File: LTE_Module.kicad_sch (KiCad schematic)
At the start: 47 parts, among them J3 USB_C_Receptacle_USB2.0_14P, J4 SIM_Card_Shielded, Q3 FDN340P, Q4 DTC143Z, Q5 DTC143Z, Q6 DTC143Z, U6 TXB0104PW, U7 SIM7080G

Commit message: fixed layout
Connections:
- no-connect marks 25 -> 26
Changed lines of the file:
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@@
+	)
+	(no_connect
+		(at 60.96 50.8)
 	)
 	(no_connect

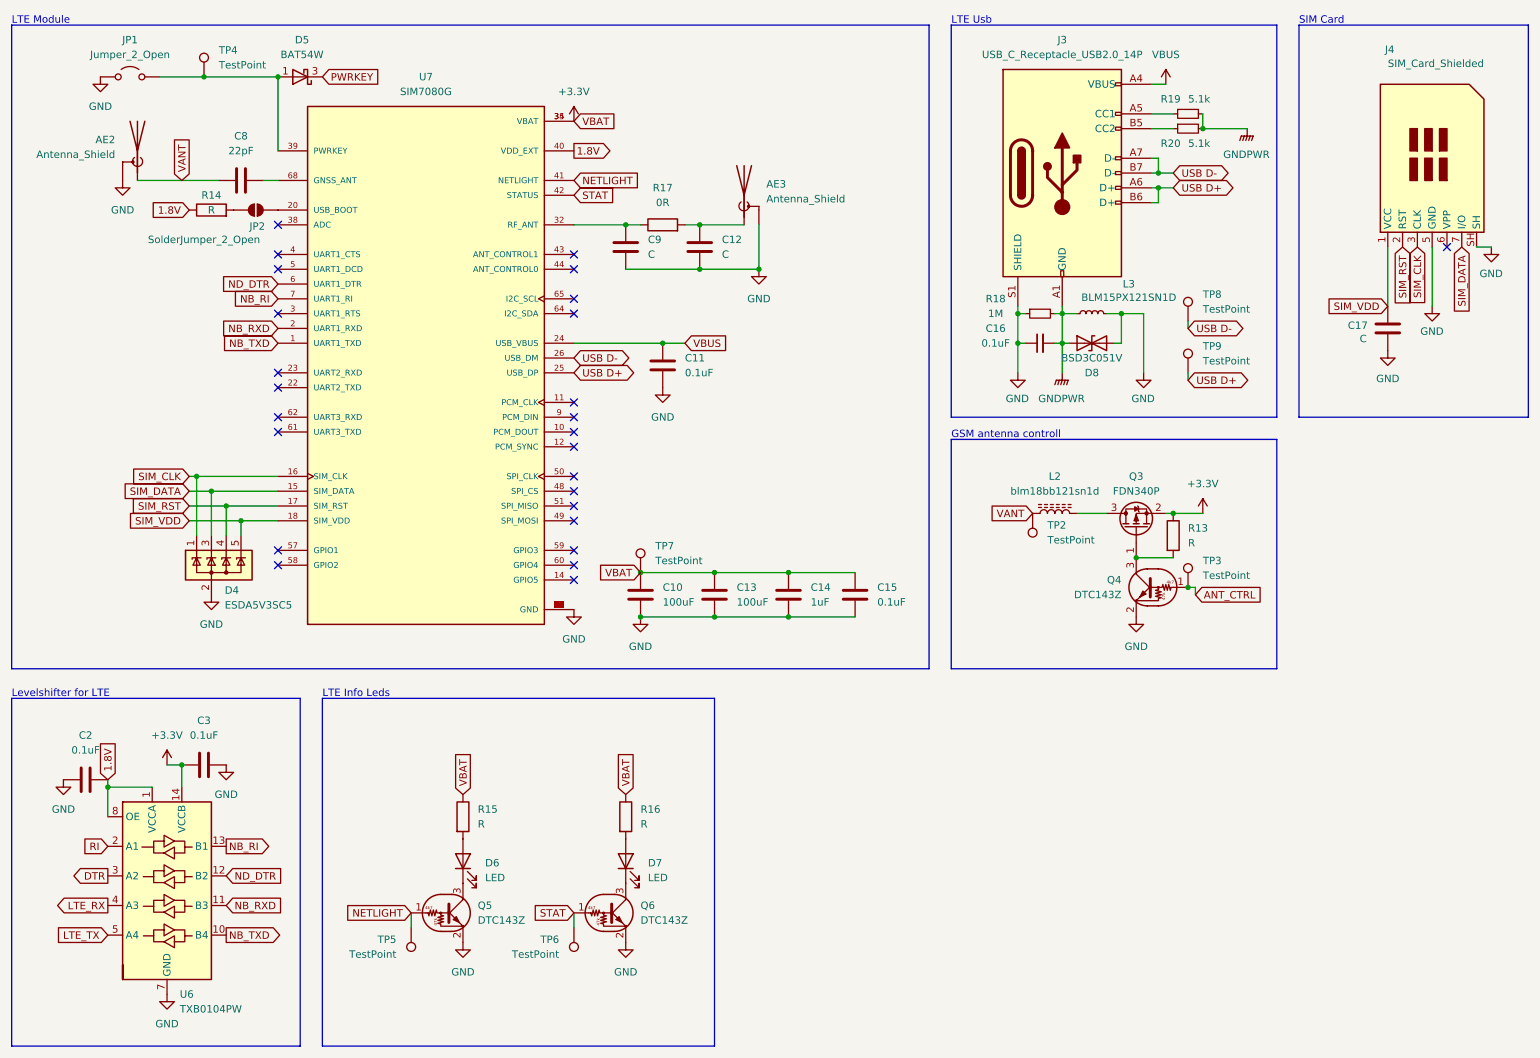
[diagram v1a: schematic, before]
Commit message: added psu and formated board outline
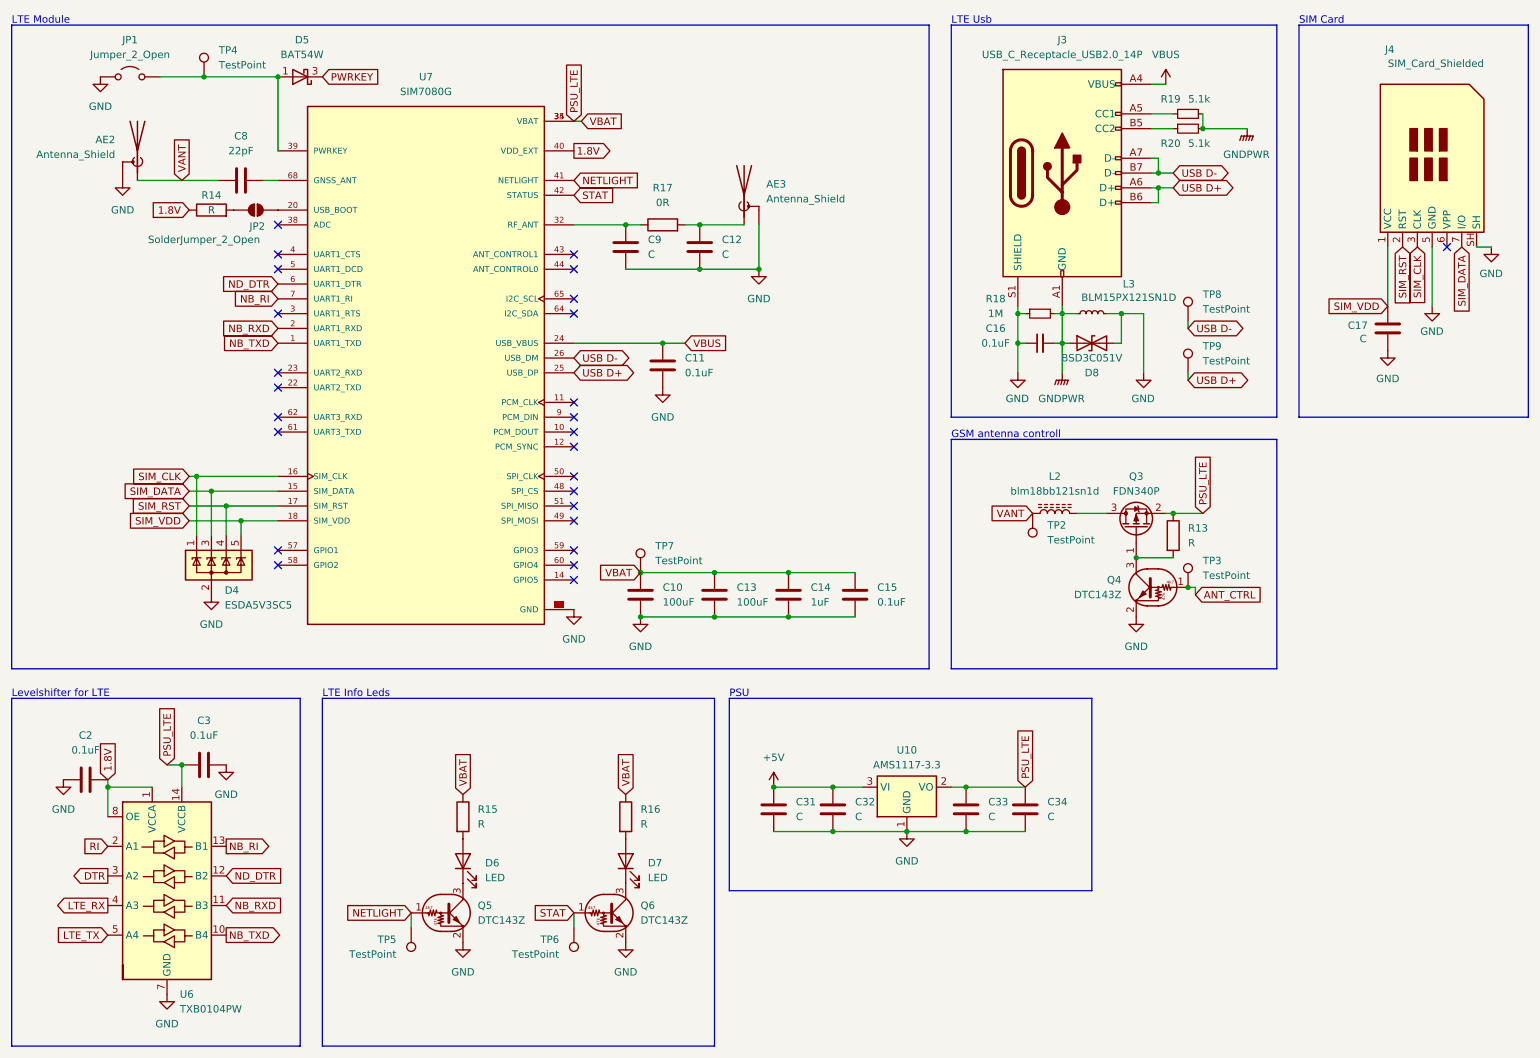
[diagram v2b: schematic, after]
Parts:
- added C31, C32, C33, C34: C, symbol Device:C
- added U10: AMS1117-3.3, Package_TO_SOT_SMD:SOT-223-3_TabPin2, symbol Regulator_Linear:AMS1117-3.3
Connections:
- net GND: now also C31.2, C32.2, C33.2, C34.2, U10.1 (GND)
- net +3.3V renamed PSU_LTE
- net PSU_LTE: now also C33.1, C34.1, U10.2 (VO)
- new net +5V: C31.1, C32.1, U10.3 (VI)
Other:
- note added: "PSU"

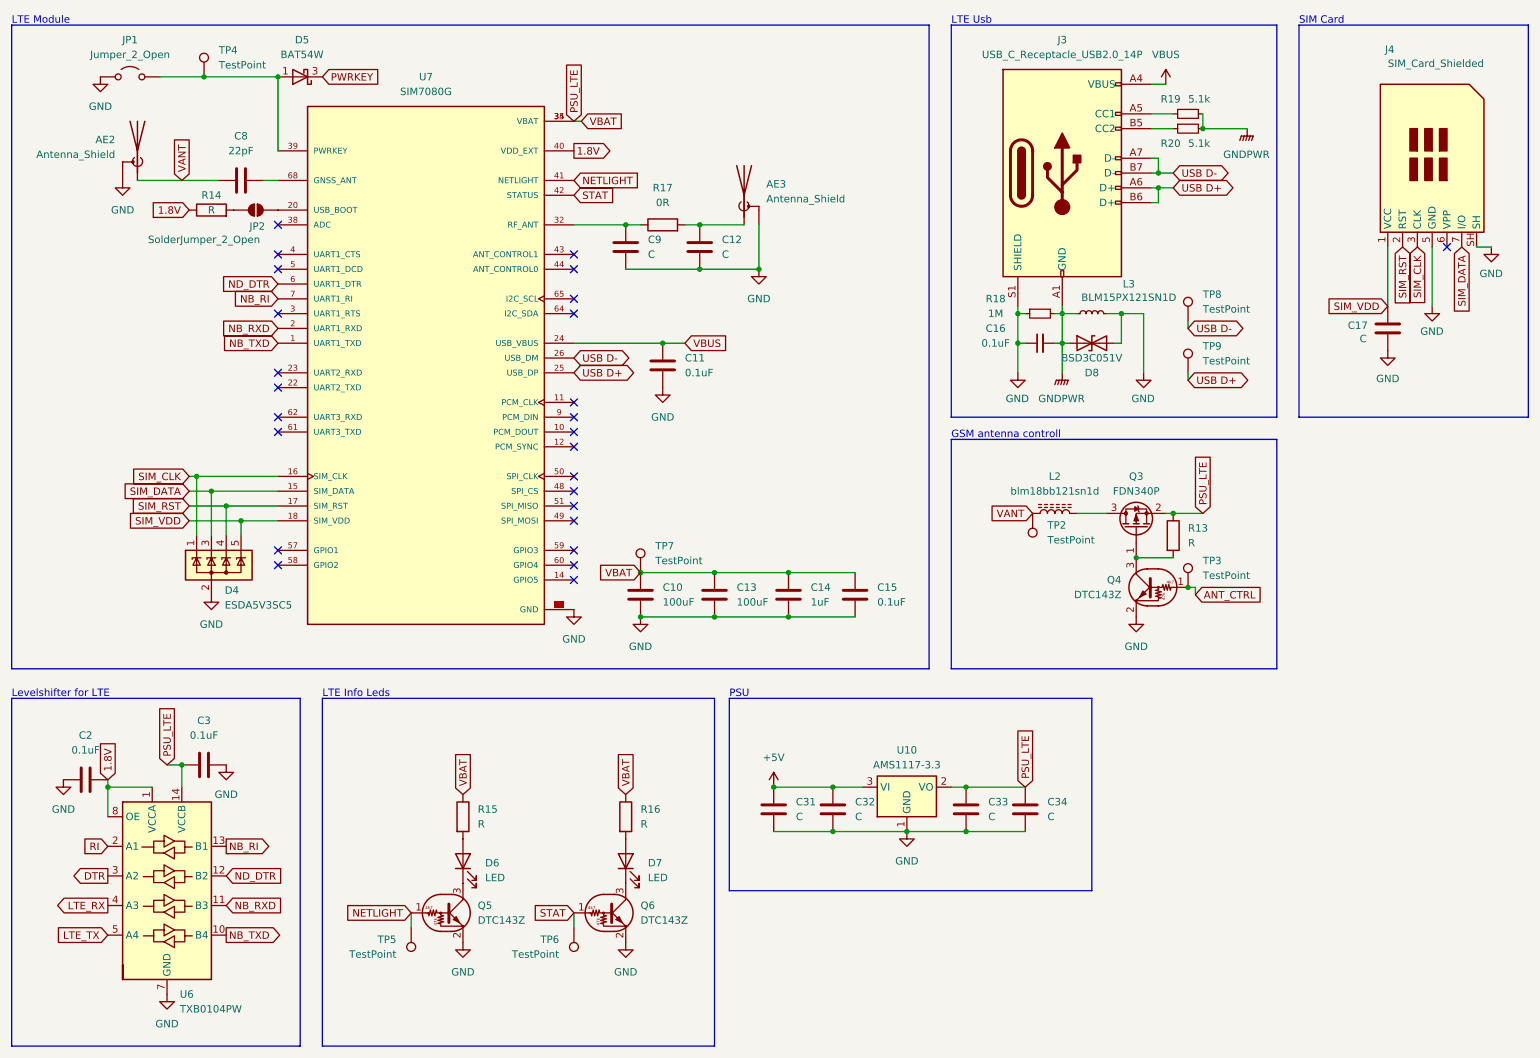
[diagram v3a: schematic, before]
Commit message: added footprint for a7670e
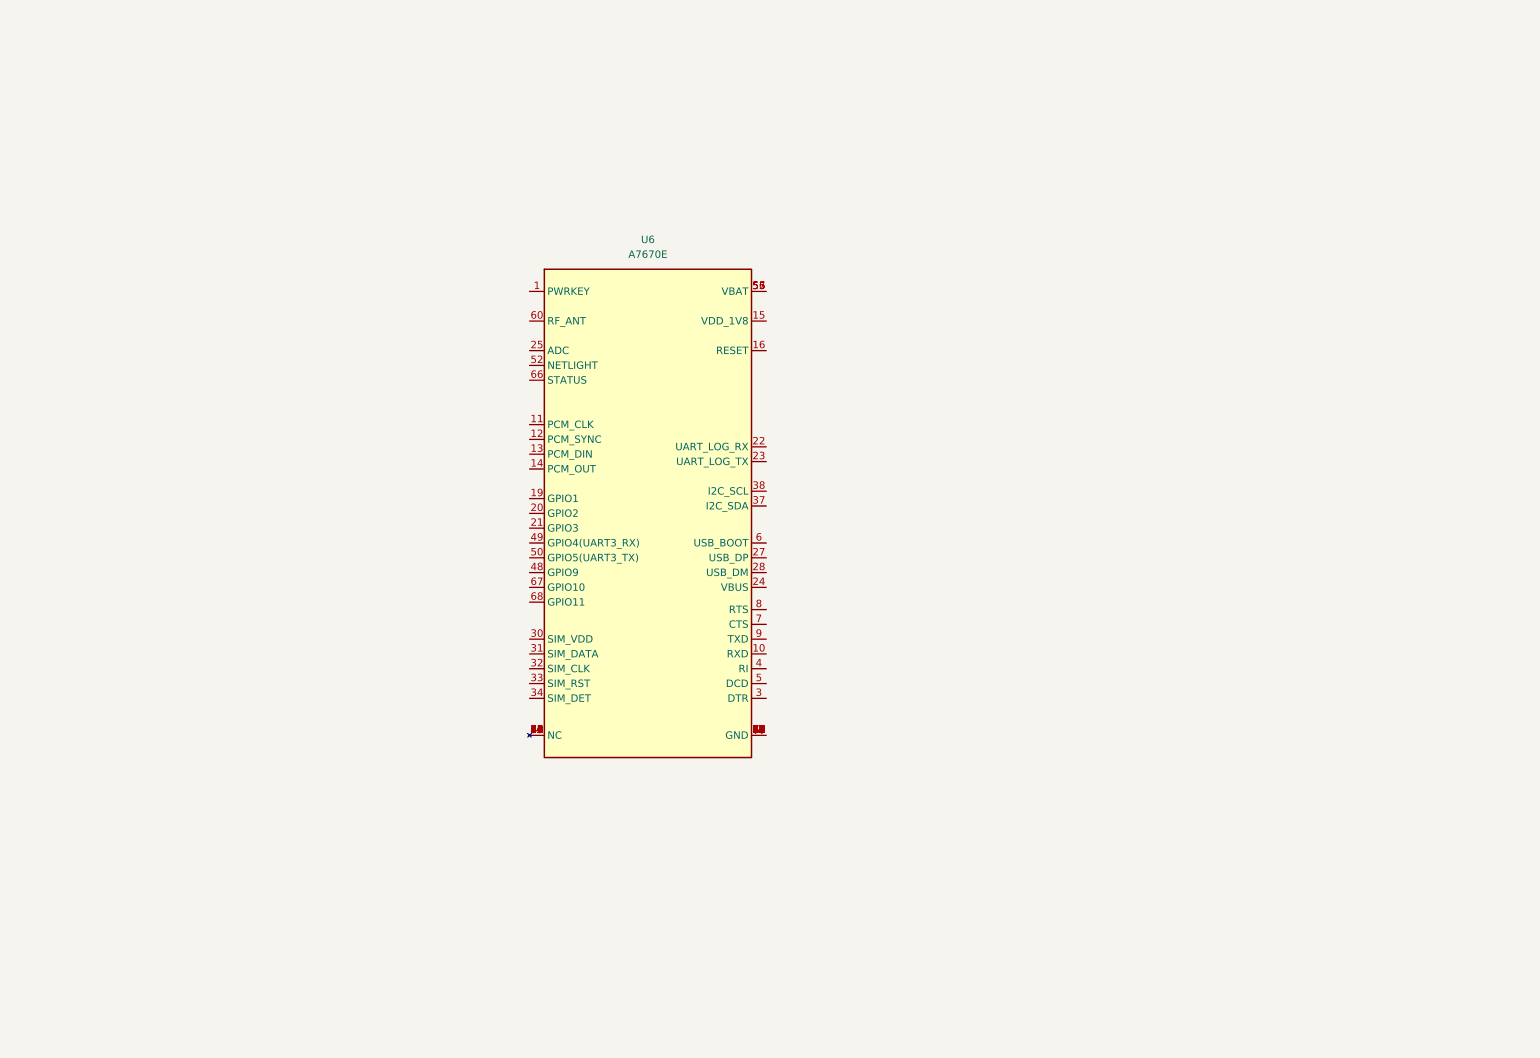
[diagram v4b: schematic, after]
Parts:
- removed AE2, AE3: Antenna_Shield, symbol Device:Antenna_Shield
- removed C10, C13: 100uF, symbol Device:C
- removed C11, C15, C2, C3: 0.1uF, symbol Device:C
- removed C12, C17, C31, C32, C33, C34, C9: C, symbol Device:C
- removed C14: 1uF, symbol Device:C
- removed C16: 0.1uF, Capacitor_SMD:C_0805_2012Metric_Pad1.18x1.45mm_HandSolder, symbol Device:C_Small
- removed C8: 22pF, symbol Device:C
- removed D4: ESDA5V3SC5, Package_TO_SOT_SMD:SOT-23-5, symbol Power_Protection:ESDA5V3SC5
- removed D5: BAT54W, Package_TO_SOT_SMD:SOT-323_SC-70, symbol Diode:BAT54W
- removed D6, D7: LED, symbol Device:LED
- removed D8: BSD3C051V, Diode_SMD:D_SOD-323, symbol Device:D_TVS
- removed J3: USB_C_Receptacle_USB2.0_14P, symbol Connector:USB_C_Receptacle_USB2.0_14P
- removed J4: SIM_Card_Shielded, symbol Connector:SIM_Card_Shielded
- removed JP1: Jumper_2_Open, symbol Jumper:Jumper_2_Open
- removed JP2: SolderJumper_2_Open, symbol Jumper:SolderJumper_2_Open
- removed L2: blm18bb121sn1d, symbol Device:L_Ferrite
- removed L3: BLM15PX121SN1D, Inductor_SMD:L_0402_1005Metric, symbol Device:L_Small
- removed Q3: FDN340P, Package_TO_SOT_SMD:SOT-23, symbol Transistor_FET:FDN340P
- removed Q4, Q5, Q6: DTC143Z, symbol Transistor_BJT:DTC143Z
- removed R13, R14, R15, R16: R, symbol Device:R
- removed R17: 0R, symbol Device:R
- removed R18: 1M, Resistor_SMD:R_1206_3216Metric_Pad1.30x1.75mm_HandSolder, symbol Device:R_Small
- removed R19, R20: 5.1k, Resistor_SMD:R_1206_3216Metric_Pad1.30x1.75mm_HandSolder, symbol Device:R_Small
- removed TP2, TP3, TP4, TP5, TP6, TP7, TP8, TP9: TestPoint, symbol Connector:TestPoint
- removed U10: AMS1117-3.3, Package_TO_SOT_SMD:SOT-223-3_TabPin2, symbol Regulator_Linear:AMS1117-3.3
- removed U6: TXB0104PW, Package_SO:TSSOP-14_4.4x5mm_P0.65mm, symbol Logic_LevelTranslator:TXB0104PW
- removed U7: SIM7080G, SIM7080G:XCVR_SIM7080G, symbol SIM7080G:SIM7080G
- added U6: A7670E, symbol a7670e:A7670E
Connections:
- new net: U6.17 (GND), U6.18 (GND), U6.2 (GND), U6.29 (GND), U6.39 (GND), U6.45 (GND), U6.46 (GND), U6.54 (GND), U6.58 (GND), U6.59 (GND), U6.61 (GND), U6.62 (GND), U6.63 (GND), U6.64 (GND), U6.65 (GND), U6.69 (GND), U6.70 (GND), U6.71 (GND), U6.72 (GND), U6.73 (GND), U6.74 (GND), U6.75 (GND), U6.76 (GND), U6.77 (GND), U6.78 (GND), U6.79 (GND), U6.80 (GND), U6.81 (GND), U6.82 (GND), U6.83 (GND), U6.84 (GND), U6.85 (GND), U6.86 (GND), U6.87 (GND), U6.88 (GND)
- new net: U6.26 (NC), U6.35 (NC), U6.36 (NC), U6.40 (NC), U6.41 (NC), U6.42 (NC), U6.43 (NC), U6.44 (NC), U6.47 (NC), U6.51 (NC), U6.53 (NC)
- new net: U6.55 (VBAT), U6.56 (VBAT), U6.57 (VBAT)
- no-connect marks 26 -> 0
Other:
- note removed: "GSM antenna controll"
- note removed: "LTE Info Leds"
- note removed: "LTE Module"
- note removed: "LTE Usb"
- note removed: "Levelshifter for LTE"
- note removed: "PSU"
- note removed: "SIM Card"

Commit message: done most of the schematics
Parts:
- added C10, C11: NC, symbol Device:C
- added C12, C15, C16: 22uF, Capacitor_SMD:C_1206_3216Metric_Pad1.33x1.80mm_HandSolder, symbol Device:C
- added C13: 120pF, symbol Device:C
- added C14, C17, C21, C24, C25, C26, C31, C32: C, symbol Device:C
- added D4, D5: LED, symbol Device:LED
- added D6: BZV55B5V1, Diode_SMD:D_MiniMELF, symbol Diode:BZV55B5V1
- added J4: Conn_Coaxial, symbol Connector:Conn_Coaxial
- added J8: SIM_Card, symbol Connector:SIM_Card
- added Q3, Q5, Q6: MMBT3904, Package_TO_SOT_SMD:SOT-23, symbol Transistor_BJT:MMBT3904
- added Q4: BC849, Package_TO_SOT_SMD:SOT-23, symbol Transistor_BJT:BC849
- added R13: R33, symbol Device:R
- added R14, R15, R16: 22R, symbol Device:R
- added R17, R43: 51R, symbol Device:R
- added R18, R48: 100K, symbol Device:R
- added R19, R20, R41, R46, R47, R49, R50: 4.7K, symbol Device:R
- added R42: 47K, symbol Device:R
- added R44, R45: 1K, symbol Device:R
- added TP11, TP12, TP17, TP2, TP7, TP8, TP9: TestPoint, symbol Connector:TestPoint
- added U9: AMS1117-3.3, Package_TO_SOT_SMD:SOT-223-3_TabPin2, symbol Regulator_Linear:AMS1117-3.3
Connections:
- net PWRKEY: now reaches U6.1 (PWRKEY)
- net PWRKEY: now also Q4.3 (C), TP2.1
- net at U6.10 (RXD): now also Q5.3 (C), R47.1
- net 1V8: now reaches U6.15 (VDD_1V8)
- net 1V8: now also R19.1, R20.2, R44.1, R45.1, R46.2, R47.2, R49.2
- net GND: now reaches U6.17 (GND), U6.18 (GND), U6.2 (GND), U6.29 (GND), U6.39 (GND), U6.45 (GND), U6.46 (GND), U6.54 (GND), U6.58 (GND), U6.59 (GND), U6.61 (GND), U6.62 (GND), U6.63 (GND), U6.64 (GND), U6.65 (GND), U6.69 (GND), U6.70 (GND), U6.71 (GND), U6.72 (GND), U6.73 (GND), U6.74 (GND), U6.75 (GND), U6.76 (GND), U6.77 (GND), U6.78 (GND), U6.79 (GND), U6.80 (GND), U6.81 (GND), U6.82 (GND), U6.83 (GND), U6.84 (GND), U6.85 (GND), U6.86 (GND), U6.87 (GND), U6.88 (GND)
- net GND: now also C10.2, C11.2, C12.2, C13.2, C14.1, C15.2, C16.2, C17.1, C21.1, C24.1, C25.2, C26.2, C31.2, C32.2, D4.1 (K), D5.1 (K), D6.2 (A), J4.2 (Ext), J8.5 (GND), R42.1, TP17.1, U9.1 (GND)
- net +5V: now reaches U6.24 (VBUS)
- net +5V: now also C25.1, C26.1, TP11.1, U9.3 (VI)
- net at U6.27 (USB_DP): now also TP8.1
- net at U6.28 (USB_DM): now also TP9.1
- net S_DTR: now reaches U6.3 (DTR)
- net S_DTR: now also Q3.3 (C), R20.1
- net SIM_VCC: now reaches U6.30 (SIM_VDD)
- net SIM_VCC: now also C13.1, J8.1 (VCC)
- net SIM_DATA: now reaches U6.31 (SIM_DATA)
- net SIM_DATA: now also C15.1, R16.2
- net SIM_CLK: now reaches U6.32 (SIM_CLK)
- net SIM_CLK: now also C16.1, R15.1
- net SIM_RST: now reaches U6.33 (SIM_RST)
- net SIM_RST: now also C12.1, R14.2
- net at U6.37 (I2C_SDA): now also R45.2
- net at U6.38 (I2C_SCL): now also R44.2
- net LED_NET: now reaches U6.52 (NETLIGHT)
- net LED_NET: now also R17.1
- net VBAT: now reaches U6.55 (VBAT), U6.56 (VBAT), U6.57 (VBAT)
- net VBAT: now also C14.2, C17.2, C21.2, C24.2, D6.1 (K), R43.1, TP12.1
- net at U6.6 (USB_BOOT): now also TP7.1
- net RP_ANT: now reaches U6.60 (RF_ANT)
- net RP_ANT: now also C10.1, R13.1
- net at U6.9 (TXD): now also Q6.2 (E)
- new net: Q4.1 (B), R41.2
- new net: Q5.1 (B), R46.1
- new net: Q3.1 (B), R19.2
- new net: C11.1, J4.1 (In), R13.2
- new net: D5.2 (A), R43.2
- new net: Q4.2 (E), R42.2
- new net: D4.2 (A), R17.2
- new net: Q6.1 (B), R49.1
- new net 3V3: C31.1, C32.1, R18.2, R48.2, R50.2, U9.2 (VO)
- new net CLK_EN: J8.3 (CLK), R15.2
- new net DATA_EN: J8.7 (I/O), R16.1
- new net DTR: Q3.2 (E), R18.1
- new net LTE_RX: Q5.2 (E), R48.1
- new net LTE_TX: Q6.3 (C), R50.1
- new net PWR: R41.1
- new net RST_EN: J8.2 (RST), R14.1
- no-connect marks 0 -> 23
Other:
- note added: "3.4~4.4V"
- note added: "A7670"
- note added: "Antenna"
- note added: "DTR"
- note added: "LEDs"
- note added: "PSU"
- note added: "PWRKEY"
- note added: "SIM_Card"
- moved on the sheet: U6

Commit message: done refacoring
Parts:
- added C33, C49: 10uF, symbol Device:C
- added C34, C50: 100pF, symbol Device:C
- added R51: 22.25K, symbol Device:R
- added R52: 10K, symbol Device:R
- added U10: MIC29302AWD, Package_TO_SOT_SMD:TO-252-5_TabPin3, symbol Regulator_Linear:MIC29302AWD
- C14, C21, C25, C31: value C -> 10uF
- C17, C24, C26, C32: value C -> 100pF
- D4, D5: footprint (none) -> Capacitor_SMD:C_0603_1608Metric
- J4: footprint (none) -> Connector_Coaxial:U.FL_Molex_MCRF_73412-0110_Vertical
- TP11, TP12, TP17, TP2, TP7, TP8, TP9: footprint (none) -> TestPoint:TestPoint_Pad_D2.5mm
- U6: footprint (none) -> A7670E:A7670E
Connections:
- net +5V: now also C33.1, C34.1, U10.1 (EN), U10.2 (VIN)
- net GND: now also C14.2, C17.2, C21.2, C24.2, C33.2, C34.2, C49.2, C50.2, R52.2, U10.3 (GND); no longer C14.1, C17.1, C21.1, C24.1
- net VBAT: now also C14.1, C17.1, C21.1, C24.1, C49.1, C50.1, R51.1, U10.4 (VOUT); no longer C14.2, C17.2, C21.2, C24.2
- new net: R51.2, R52.1, U10.5 (ADJ)
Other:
- note added: "VABT = 3.4~4.4V"
- note removed: "3.4~4.4V"
- moved on the sheet: D6
